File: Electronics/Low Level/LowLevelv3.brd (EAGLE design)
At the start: 117.1 x 67.6 mm, 71 parts, among them IC1_2515 MCP2515, IC2_2551 MCP2551DIL08, IC3_4802 MCP4802, Q1 16MHz, T1 2N3904, T2 2N3904, X1 284512-4, X3 Motor, X4 CLICK

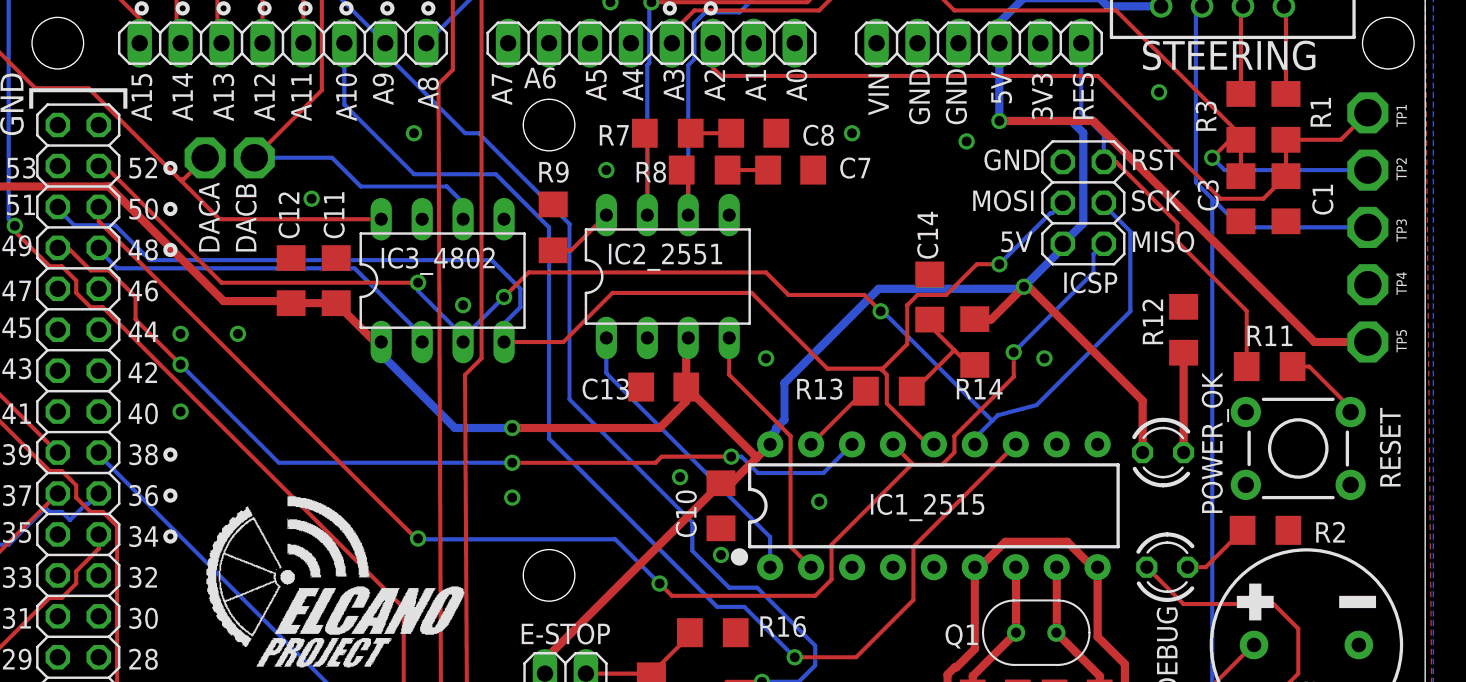
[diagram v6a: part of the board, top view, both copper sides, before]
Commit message: Minorsilkscreen updates
Named testpoints
Swapped 10k for 0 ohm resistor on reset button
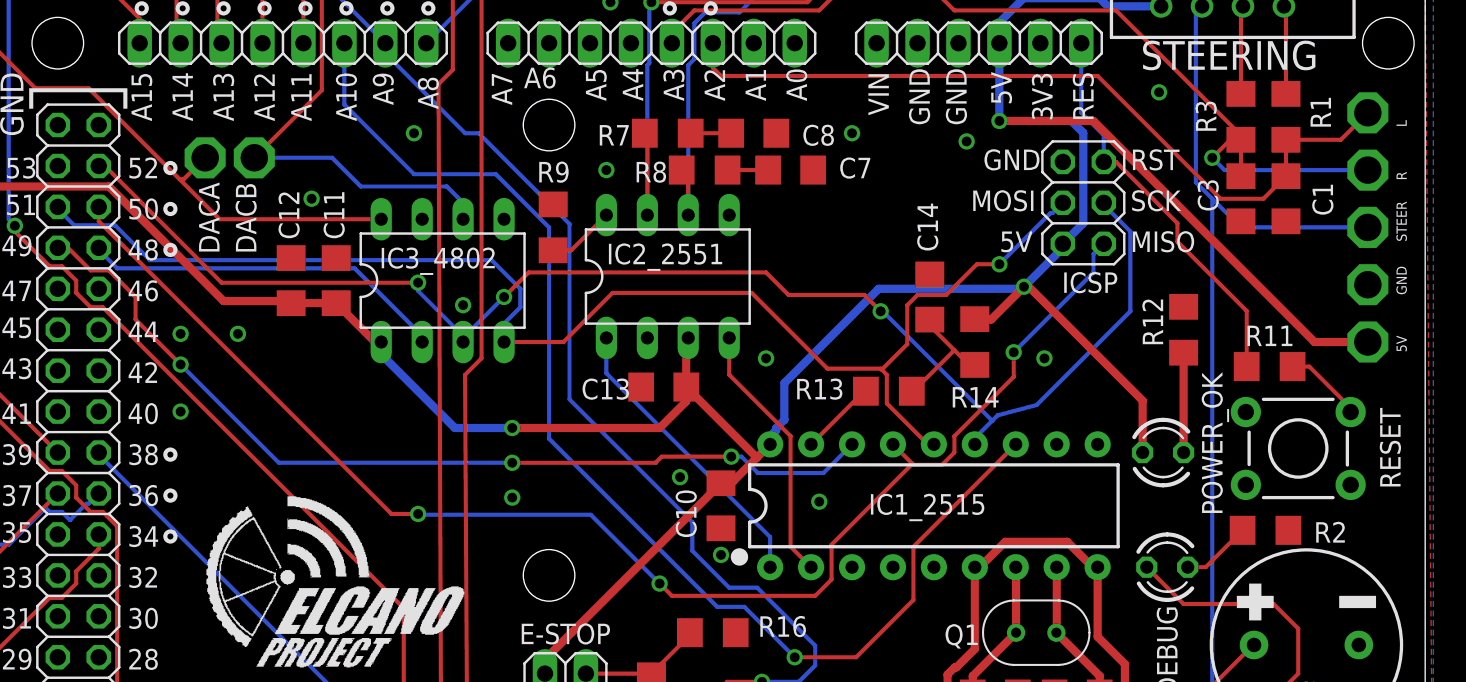
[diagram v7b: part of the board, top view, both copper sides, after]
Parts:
- R11: value 10k -> 0
- renumbered TP1 to L, TP2 to R, TP3 to STEER, TP4 to GND, TP5 to 5V
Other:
- board text added: "Click"
- board text added: "Steering"
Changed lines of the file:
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@@
 3
 1</text>
+<text x="111.252" y="67.31" size="1.778" layer="26" rot="MR0">Steering</text>
+<text x="97.282" y="69.088" size="1.524" layer="26" rot="MR270">Click</text>
 </plain>
 <attributes>
@@
 <attribute name="SF_SKU" value="COM-00097" x="109.22" y="28.194" size="1.778" layer="27" rot="R180" display="off"/>
 </element>
-<element name="R11" library="resistor" library_urn="urn:adsk.eagle:library:348" package="R1206" package3d_urn="urn:adsk.eagle:package:23540/2" value="10k" x="107.442" y="33.274" smashed="yes">
+<element name="R11" library="resistor" library_urn="urn:adsk.eagle:library:348" package="R1206" package3d_urn="urn:adsk.eagle:package:23540/2" value="0" x="107.442" y="33.274" smashed="yes">
 <attribute name="NAME" x="105.918" y="34.544" size="1.27" layer="25" ratio="10"/>
 <attribute name="VALUE" x="109.7534" y="34.925" size="0.635" layer="27" ratio="10"/>
@@
 </element>
 <element name="C14" library="resistor" library_urn="urn:adsk.eagle:library:348" package="C1206" package3d_urn="urn:adsk.eagle:package:23618/2" value="0.1uF" x="86.36" y="37.592" smashed="yes" rot="R90">
-<attribute name="NAME" x="86.868" y="39.878" size="1.27" layer="25" ratio="10" rot="R90"/>
+<attribute name="NAME" x="86.868" y="40.386" size="1.27" layer="25" ratio="10" rot="R90"/>
 <attribute name="VALUE" x="86.614" y="43.942" size="0.635" layer="27" ratio="10" rot="R90"/>
 </element>
@@
 </element>
 <element name="R14" library="resistor" library_urn="urn:adsk.eagle:library:348" package="R1206" package3d_urn="urn:adsk.eagle:package:23540/2" value="20K" x="89.154" y="34.798" smashed="yes" rot="R270">
-<attribute name="NAME" x="87.884" y="31.242" size="1.27" layer="25" ratio="10"/>
+<attribute name="NAME" x="87.63" y="30.734" size="1.27" layer="25" ratio="10"/>
 <attribute name="VALUE" x="88.6714" y="30.353" size="0.635" layer="27" ratio="10"/>
 </element>
@@
 <attribute name="VALUE" x="112.649" y="61.976" size="1.778" layer="27" rot="R180"/>
 </element>
-<element name="TP1" library="testpad" library_urn="urn:adsk.eagle:library:385" package="P1-17" package3d_urn="urn:adsk.eagle:package:27949/1" value="PTR1PAD1-17" x="113.538" y="49.022" smashed="yes">
+<element name="L" library="testpad" library_urn="urn:adsk.eagle:library:385" package="P1-17" package3d_urn="urn:adsk.eagle:package:27949/1" value="PTR1PAD1-17" x="113.538" y="49.022" smashed="yes">
 <attribute name="NAME" x="115.951" y="48.133" size="0.635" layer="25" ratio="10" rot="R90"/>
 <attribute name="TP_SIGNAL_NAME" value="" x="113.538" y="49.022" size="1.778" layer="27" display="off"/>
 <attribute name="VALUE" x="113.284" y="49.022" size="0.0254" layer="27"/>
 </element>
-<element name="TP2" library="testpad" library_urn="urn:adsk.eagle:library:385" package="P1-17" package3d_urn="urn:adsk.eagle:package:27949/1" value="PTR1PAD1-17" x="113.538" y="45.466" smashed="yes">
+<element name="R" library="testpad" library_urn="urn:adsk.eagle:library:385" package="P1-17" package3d_urn="urn:adsk.eagle:package:27949/1" value="PTR1PAD1-17" x="113.538" y="45.466" smashed="yes">
 <attribute name="NAME" x="115.951" y="44.831" size="0.635" layer="25" ratio="10" rot="R90"/>
 <attribute name="TP_SIGNAL_NAME" value="" x="112.268" y="42.291" size="1" layer="37"/>
 <attribute name="VALUE" x="113.538" y="44.196" size="0.0254" layer="27"/>
 </element>
-<element name="TP3" library="testpad" library_urn="urn:adsk.eagle:library:385" package="P1-17" package3d_urn="urn:adsk.eagle:package:27949/1" value="PTR1PAD1-17" x="113.538" y="41.91" smashed="yes">
+<element name="STEER" library="testpad" library_urn="urn:adsk.eagle:library:385" package="P1-17" package3d_urn="urn:adsk.eagle:package:27949/1" value="PTR1PAD1-17" x="113.538" y="41.91" smashed="yes">
 <attribute name="NAME" x="115.951" y="41.021" size="0.635" layer="25" ratio="10" rot="R90"/>
 <attribute name="TP_SIGNAL_NAME" value="" x="112.268" y="38.735" size="1" layer="37"/>
 <attribute name="VALUE" x="113.538" y="40.894" size="0.0254" layer="27"/>
 </element>
-<element name="TP4" library="testpad" library_urn="urn:adsk.eagle:library:385" package="P1-17" package3d_urn="urn:adsk.eagle:package:27949/1" value="PTR1PAD1-17" x="113.538" y="38.354" smashed="yes">
+<element name="GND" library="testpad" library_urn="urn:adsk.eagle:library:385" package="P1-17" package3d_urn="urn:adsk.eagle:package:27949/1" value="PTR1PAD1-17" x="113.538" y="38.354" smashed="yes">
 <attribute name="NAME" x="115.951" y="37.719" size="0.635" layer="25" ratio="10" rot="R90"/>
 <attribute name="TP_SIGNAL_NAME" value="" x="112.268" y="35.179" size="1" layer="37"/>
 <attribute name="VALUE" x="113.538" y="38.608" size="0.0254" layer="27"/>
 </element>
-<element name="TP5" library="testpad" library_urn="urn:adsk.eagle:library:385" package="P1-17" package3d_urn="urn:adsk.eagle:package:27949/1" value="PTR1PAD1-17" x="113.538" y="34.798" smashed="yes">
+<element name="5V" library="testpad" library_urn="urn:adsk.eagle:library:385" package="P1-17" package3d_urn="urn:adsk.eagle:package:27949/1" value="PTR1PAD1-17" x="113.538" y="34.798" smashed="yes">
 <attribute name="NAME" x="115.951" y="34.163" size="0.635" layer="25" ratio="10" rot="R90"/>
 <attribute name="TP_SIGNAL_NAME" value="" x="113.538" y="34.798" size="1.778" layer="27" display="off"/>
@@
 <contactref element="STEERING" pad="1"/>
 <via x="100.584" y="50.292" extent="1-16" drill="0.6096"/>
-<contactref element="TP4" pad="TP"/>
+<contactref element="GND" pad="TP"/>
 <contactref element="R2" pad="1"/>
 <wire x1="104.521" y1="61.595" x2="104.521" y2="58.166" width="0.508" layer="16"/>
@@
 <wire x1="97.409" y1="55.626" x2="96.901" y2="56.134" width="0.508" layer="16"/>
 <wire x1="96.901" y1="56.134" x2="92.18394375" y2="56.134" width="0.508" layer="16"/>
-<contactref element="TP5" pad="TP"/>
+<contactref element="5V" pad="TP"/>
 <wire x1="110.22758125" y1="34.798" x2="96.51158125" y2="48.514" width="0.508" layer="1"/>
 <wire x1="113.538" y1="34.798" x2="110.22758125" y2="34.798" width="0.508" layer="1"/>
@@
 <via x="91.567" y="34.163" extent="1-16" drill="0.6096"/>
 <wire x1="79.248" y1="19.05" x2="80.264" y2="20.066" width="0.254" layer="1"/>
-<wire x1="54.61" y1="22.606" x2="54.483" y2="22.606" width="0.254" layer="1"/>
-<wire x1="54.483" y1="22.606" x2="34.798" y2="42.291" width="0.254" layer="1"/>
-<via x="54.61" y="22.606" extent="1-16" drill="0.6096"/>
+<wire x1="54.61" y1="24.13" x2="52.959" y2="24.13" width="0.254" layer="1"/>
+<wire x1="52.959" y1="24.13" x2="34.798" y2="42.291" width="0.254" layer="1"/>
+<via x="54.61" y="24.13" extent="1-16" drill="0.6096"/>
 <via x="69.596" y="19.812" extent="1-16" drill="0.6096"/>
-<wire x1="66.853" y1="22.555" x2="54.61" y2="22.555" width="0.254" layer="16"/>
-<wire x1="54.61" y1="22.606" x2="54.61" y2="22.555" width="0.254" layer="16"/>
-<wire x1="66.853" y1="22.555" x2="69.596" y2="19.812" width="0.254" layer="16"/>
+<wire x1="65.329" y1="24.079" x2="54.61" y2="24.079" width="0.254" layer="16"/>
+<wire x1="54.61" y1="24.13" x2="54.61" y2="24.079" width="0.254" layer="16"/>
+<wire x1="65.329" y1="24.079" x2="69.596" y2="19.812" width="0.254" layer="16"/>
 <wire x1="69.596" y1="19.812" x2="70.358" y2="19.05" width="0.254" layer="1"/>
 <wire x1="70.358" y1="19.05" x2="79.248" y2="19.05" width="0.254" layer="1"/>
@@
 <wire x1="103.886" y1="43.688" x2="103.886" y2="11.176" width="0.254" layer="16"/>
 <wire x1="80.518" y1="7.366" x2="82.042" y2="8.89" width="0.254" layer="16"/>
-<contactref element="TP3" pad="TP"/>
+<contactref element="STEER" pad="TP"/>
 <wire x1="113.538" y1="41.91" x2="105.664" y2="41.91" width="0.254" layer="16"/>
 <wire x1="105.664" y1="41.91" x2="103.886" y2="43.688" width="0.254" layer="16"/>
@@
 <wire x1="105.664" y1="47.346" x2="105.664" y2="47.625" width="0.254" layer="1"/>
 <wire x1="105.664" y1="47.625" x2="97.917" y2="55.372" width="0.254" layer="1"/>
-<contactref element="TP2" pad="TP"/>
+<contactref element="R" pad="TP"/>
 <wire x1="113.538" y1="45.466" x2="104.648" y2="45.466" width="0.254" layer="16"/>
 <wire x1="104.648" y1="45.466" x2="103.886" y2="46.228" width="0.254" layer="16"/>
@@
 <wire x1="96.774" y1="51.308" x2="104.394" y2="43.688" width="0.254" layer="1"/>
 <wire x1="104.394" y1="43.688" x2="107.058" y2="43.688" width="0.254" layer="1"/>
-<contactref element="TP1" pad="TP"/>
+<contactref element="L" pad="TP"/>
 <wire x1="108.458" y1="47.346" x2="111.862" y2="47.346" width="0.254" layer="1"/>
 <wire x1="111.862" y1="47.346" x2="113.538" y2="49.022" width="0.254" layer="1"/>
